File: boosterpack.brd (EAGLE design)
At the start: 71.4 x 44.4 mm, 39 parts, among them J1 POWERPOLE_DOUBLE, J2 PHOENIXSCREWTERMINAL_2, J3 PHOENIXSCREWTERMINAL_2

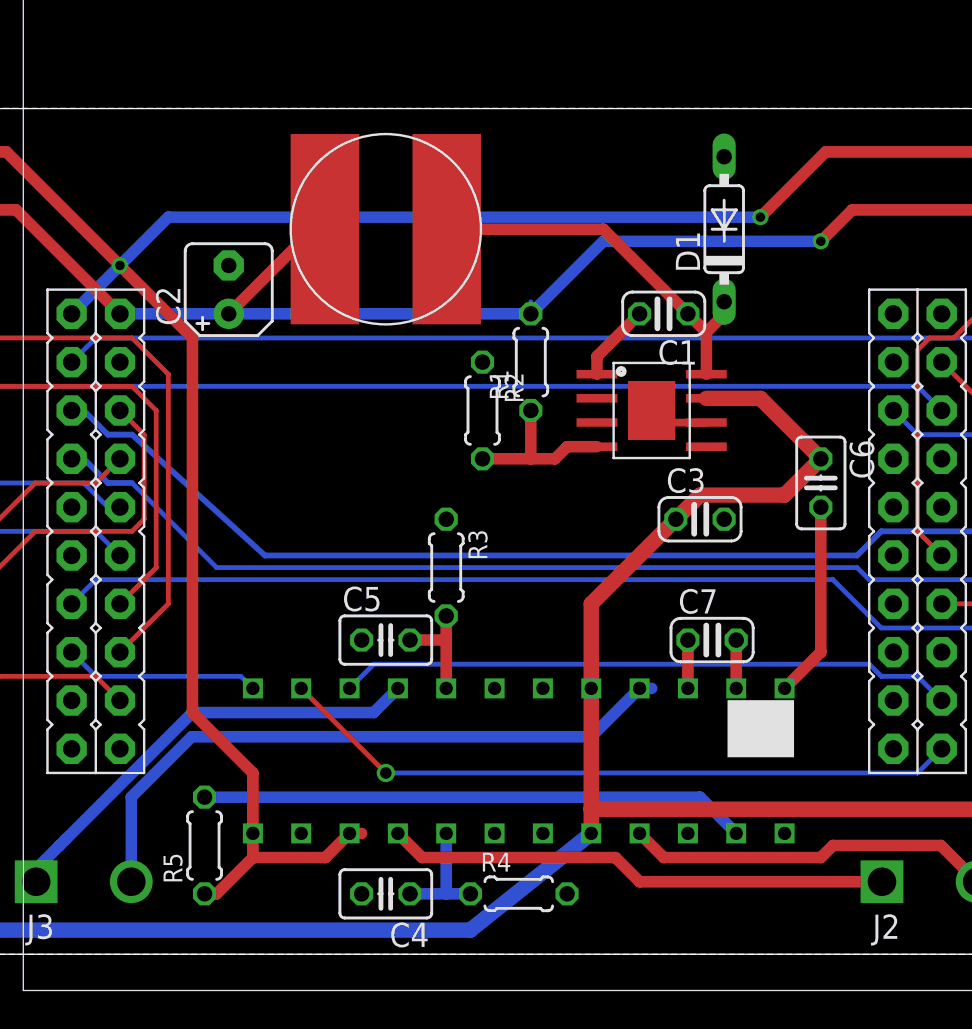
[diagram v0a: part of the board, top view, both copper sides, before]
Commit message: increased the spacing between the leads of all resistors and some caps
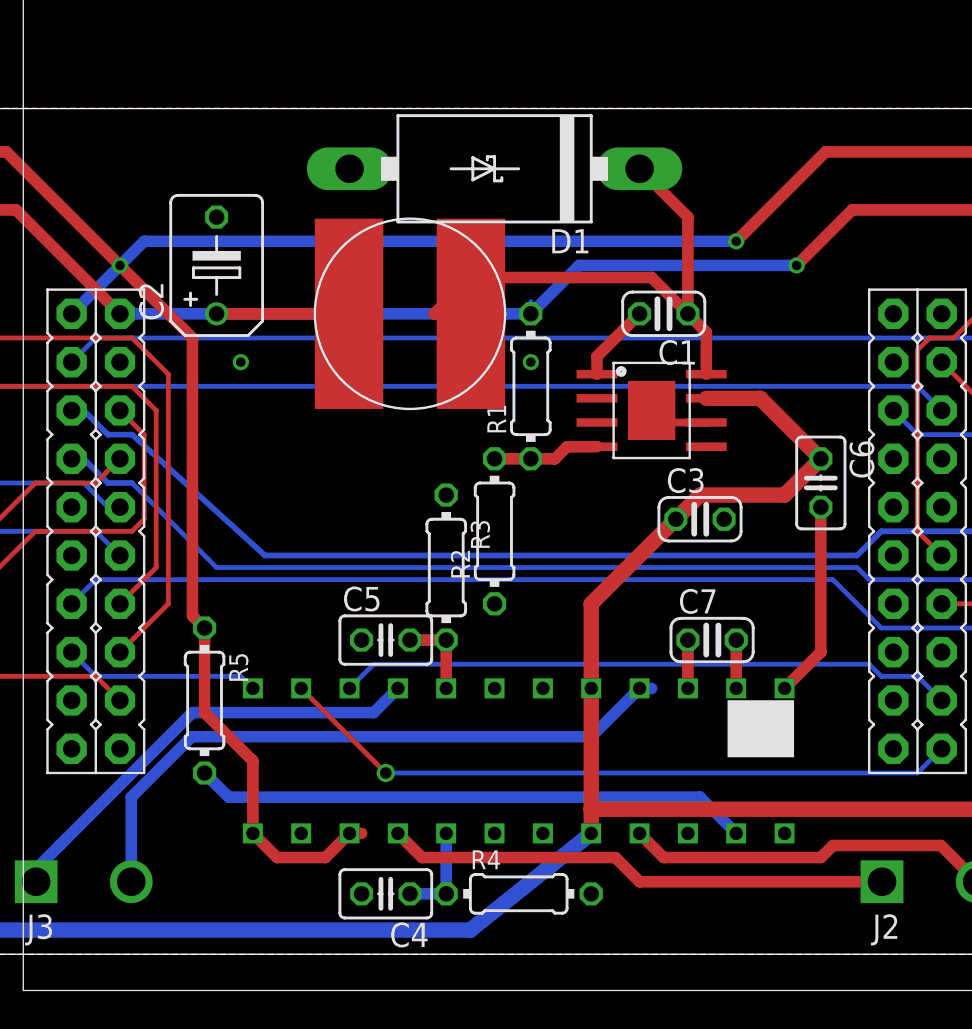
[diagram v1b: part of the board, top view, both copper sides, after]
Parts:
- C2: device resistor:B45181A -> rcl:B45181B
- D1: device diode:DO35-7 -> diode:DO201T15
- R1, R2, R3, R4, R5: device resistor:0204/5 -> rcl:0204/7
- moved D1 12.5 mm to (47.6, 68.6), turned to 180 degrees
- moved R5 7.62 mm to (32.4, 40.6), turned to 270 degrees
- moved R2 6.38 mm to (47.6, 49.5), turned to 90 degrees
- moved L1 4.62 mm to (43.2, 61.0)
- moved C2 1.42 mm to (33.0, 63.5)
- moved R1 1.27 mm to (49.5, 57.1)
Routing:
- net N$11: track 20.1 -> 29.1 mm
- net +3V3: track 110.0 -> 105.9 mm
- net N$10: track 8.82 -> 5.64 mm
- net N$19: track 5.72 -> 4.45 mm
- net N$20: track 6.35 -> 5.08 mm
- net N$22: track 28.7 -> 29.3 mm
- net GND: vias 0 -> 2
